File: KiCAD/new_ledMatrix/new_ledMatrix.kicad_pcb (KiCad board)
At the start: 2 copper layers, 72.6 x 39.1 mm, 61 parts

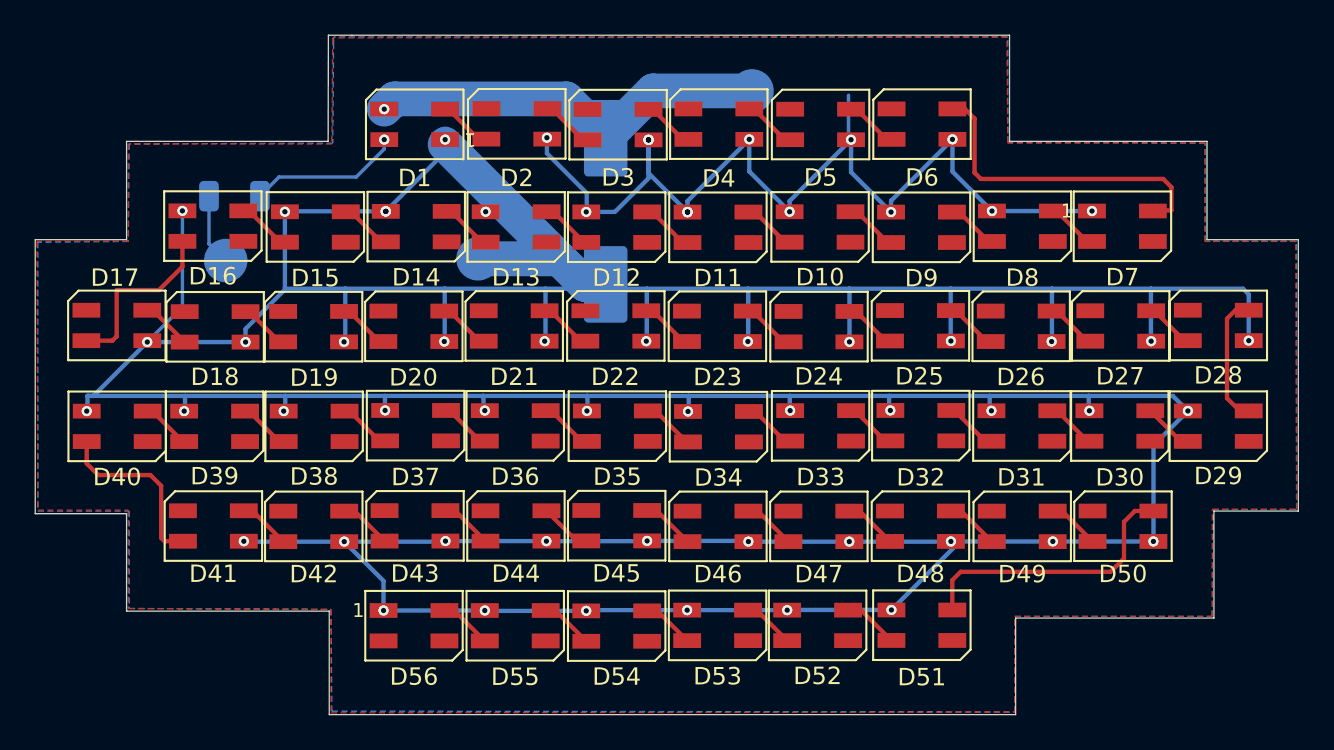
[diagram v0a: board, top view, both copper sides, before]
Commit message: added DOUT in PCB
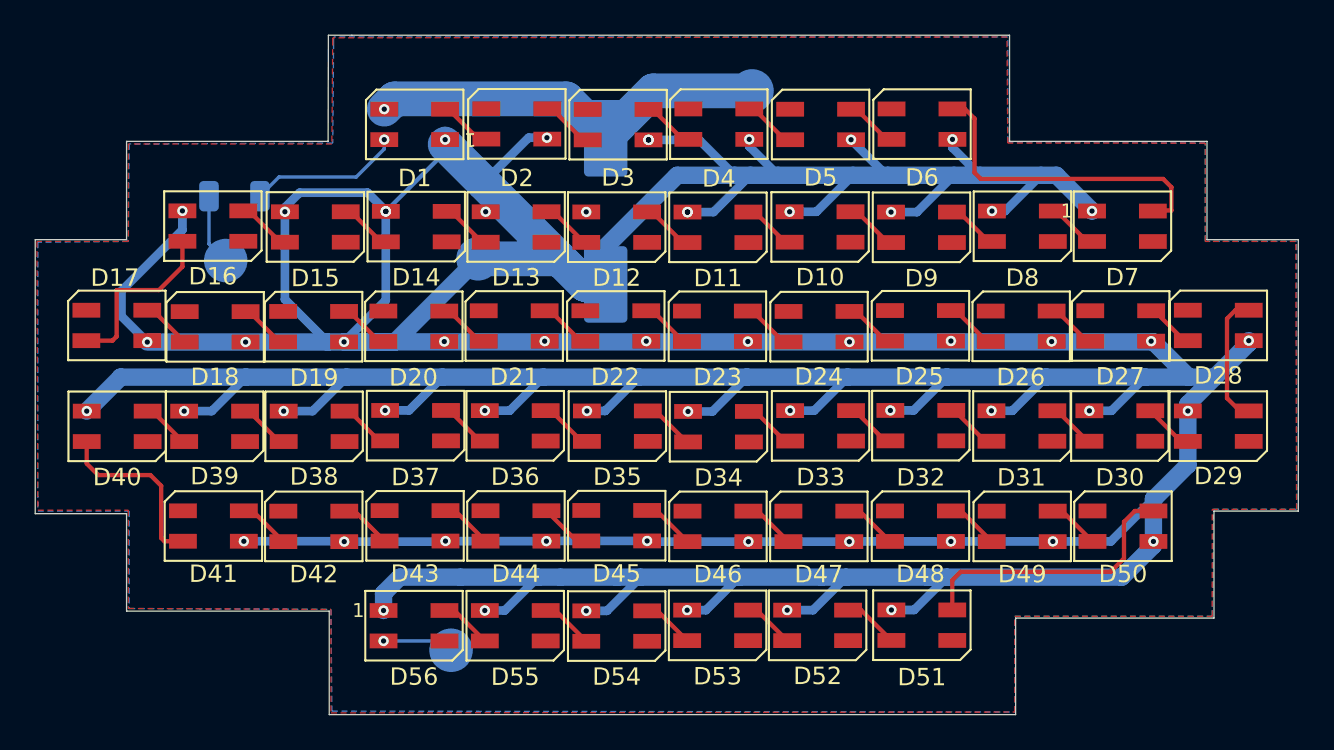
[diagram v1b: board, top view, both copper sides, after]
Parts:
- added TP4: DOUT, TestPoint:TestPoint_Pad_D2.5mm, B.Cu at (124.2, 94.2)
- C1: value 1000uF -> 1000uF(10x10.5mm)
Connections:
- D56 pad 2: unconnected-(D56-DOUT-Pad2) -> Net-(D56-DOUT)
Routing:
- net +5V: track 379.1 -> 504.8 mm
- net Net-(D56-DOUT): track 0.00 -> 4.10 mm, vias 0 -> 1
